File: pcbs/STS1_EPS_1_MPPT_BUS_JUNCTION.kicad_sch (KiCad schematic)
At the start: 26 parts, among them Q2 SI7135DP-T1-GE3, Q3 SI7135DP-T1-GE3, U11 INA180A4, U13 TPS259472ARPW, U19 TPS259472ARPW, U20 TPS259472ARPW, U21 TPS259472ARPW, U22 TPS259472ARPW, U23 TPS259472ARPW, U24 TPS259472ARPW, U4 TPS259472ARPW

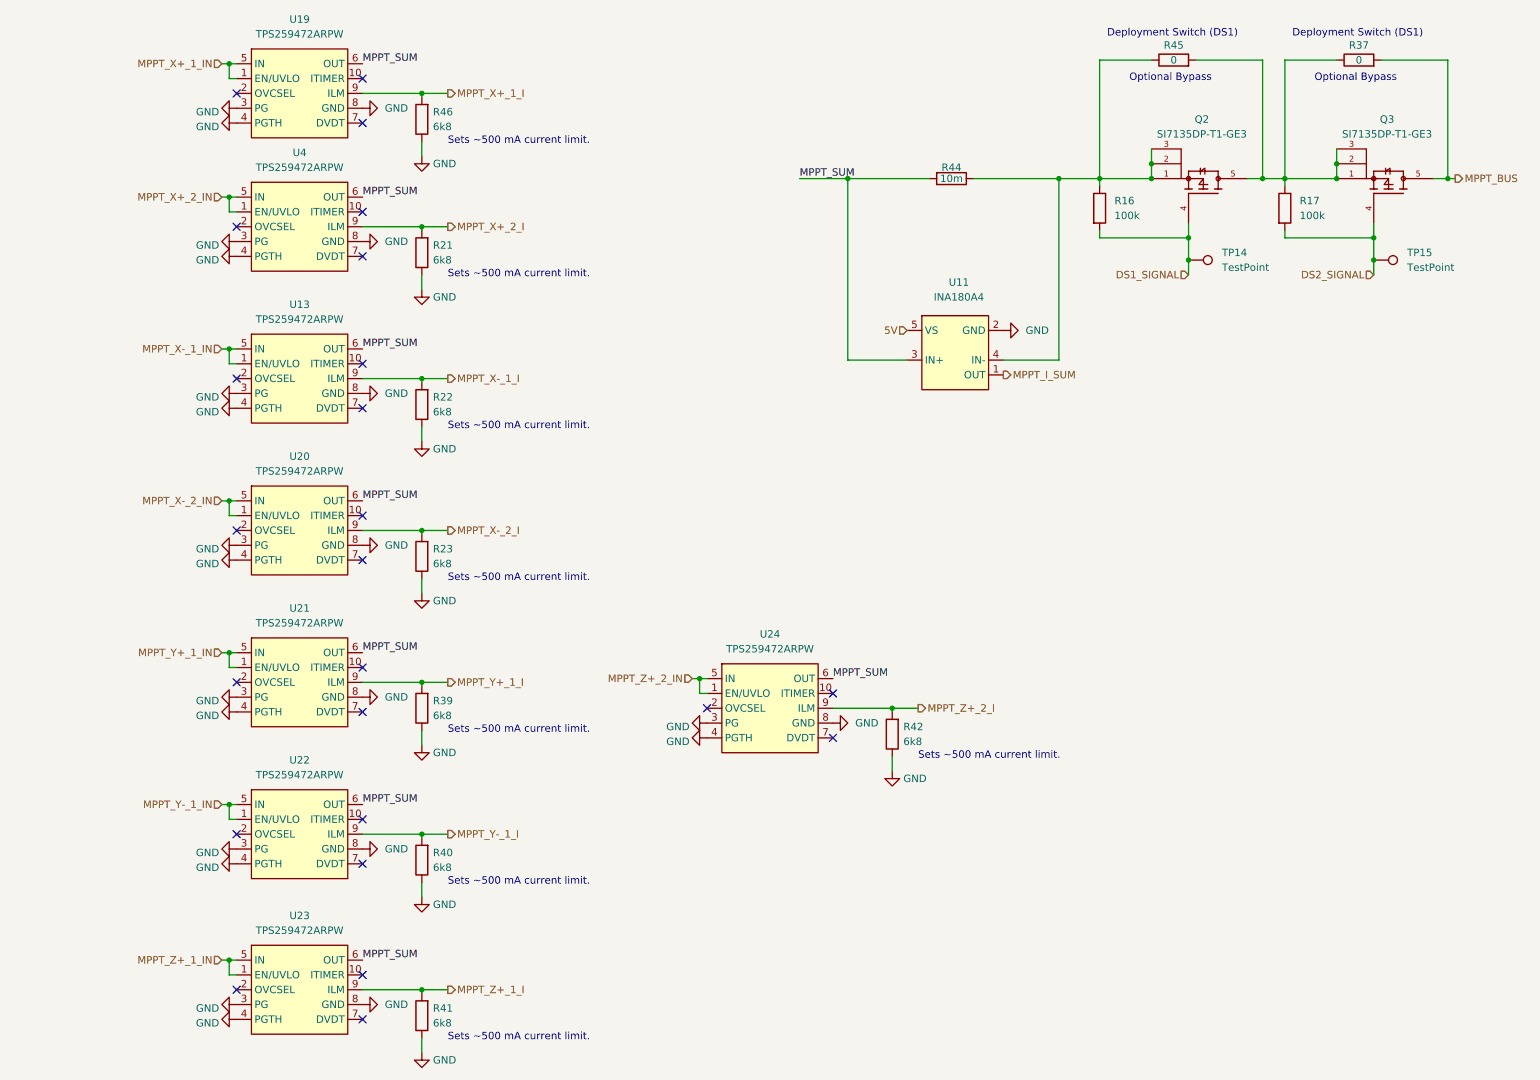
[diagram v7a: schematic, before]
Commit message: Worked on STS1_EPS_1.
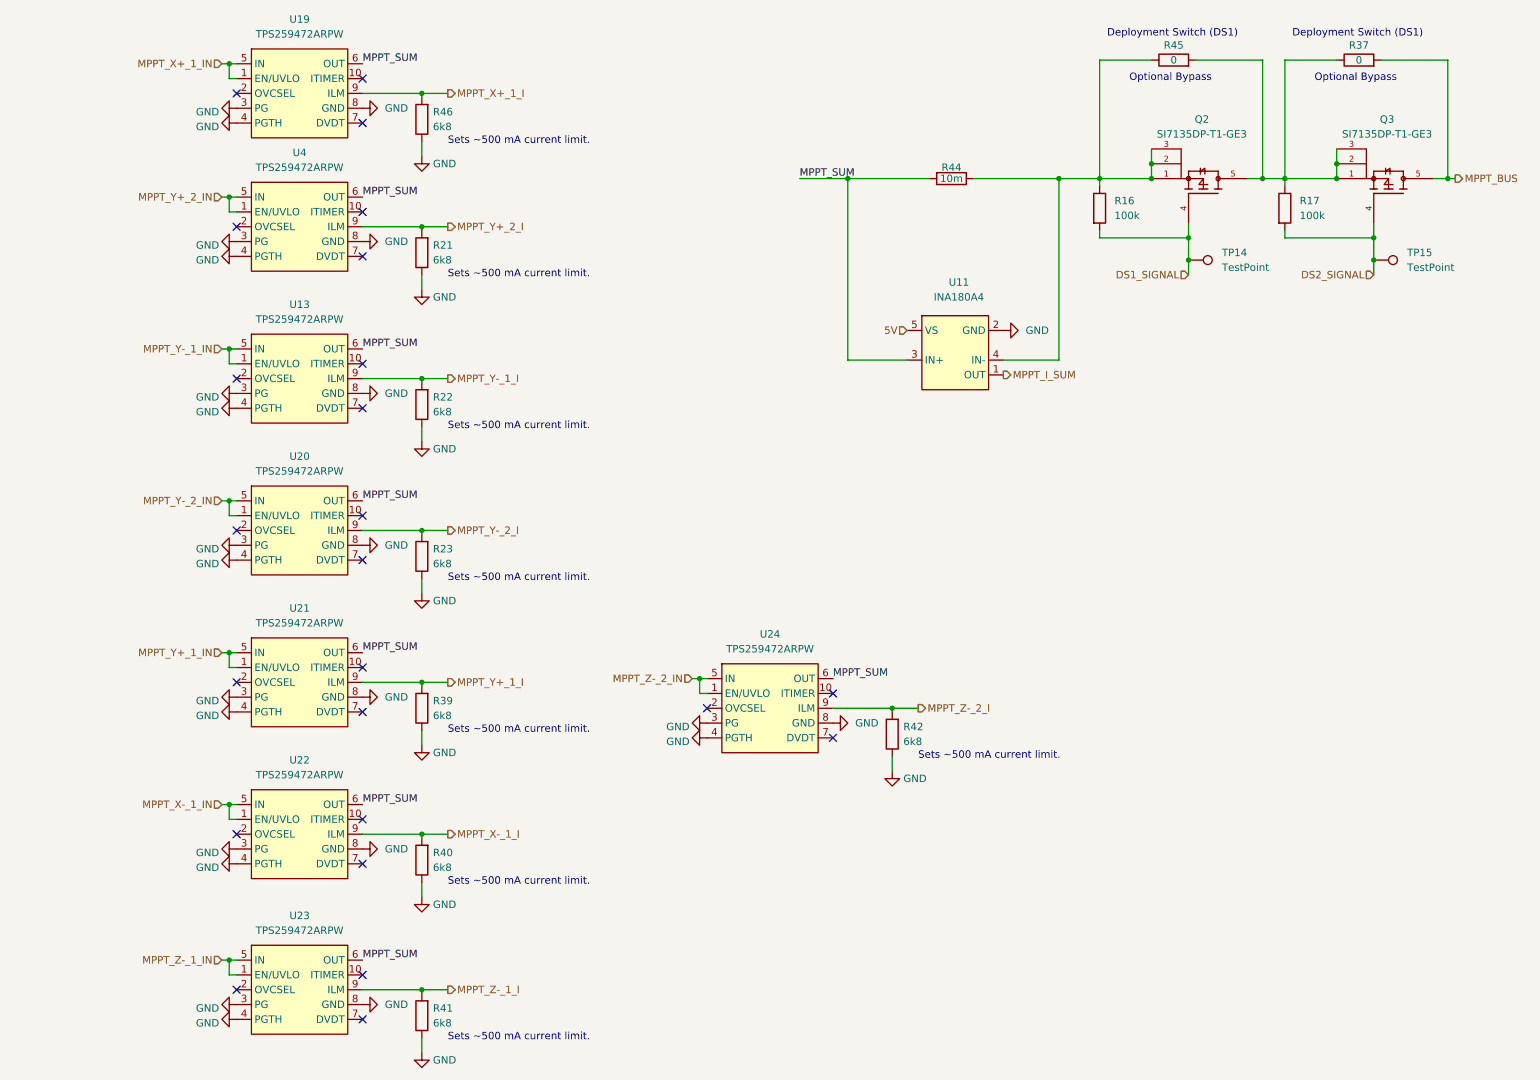
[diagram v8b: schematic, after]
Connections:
- net MPPT_X-_1_I: now also R40.2, U22.9 (ILM); no longer R22.2, U13.9 (ILM)
- net MPPT_X-_1_IN: now also U22.1 (EN/UVLO), U22.5 (IN); no longer U13.1 (EN/UVLO), U13.5 (IN)
- net MPPT_Y-_1_I: now also R22.2, U13.9 (ILM); no longer R40.2, U22.9 (ILM)
- net MPPT_Y-_1_IN: now also U13.1 (EN/UVLO), U13.5 (IN); no longer U22.1 (EN/UVLO), U22.5 (IN)
- net MPPT_X+_2_I renamed MPPT_Y+_2_I
- net MPPT_X+_2_IN renamed MPPT_Y+_2_IN
- net MPPT_X-_2_I renamed MPPT_Y-_2_I
- net MPPT_X-_2_IN renamed MPPT_Y-_2_IN
- net MPPT_Z+_1_I renamed MPPT_Z-_1_I
- net MPPT_Z+_1_IN renamed MPPT_Z-_1_IN
- net MPPT_Z+_2_I renamed MPPT_Z-_2_I
- net MPPT_Z+_2_IN renamed MPPT_Z-_2_IN
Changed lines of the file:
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@@
     (effects (font (size 1.27 1.27)) (justify left))
   )
-  (hierarchical_label "MPPT_Y-_1_I" (shape output) (at 86.36 155.575 0)
+  (hierarchical_label "MPPT_X-_1_I" (shape output) (at 86.36 155.575 0)
     (effects (font (size 1.27 1.27)) (justify left))
   )
-  (hierarchical_label "MPPT_Z+_1_I" (shape output) (at 86.36 182.245 0)
+  (hierarchical_label "MPPT_Z-_1_I" (shape output) (at 86.36 182.245 0)
     (effects (font (size 1.27 1.27)) (justify left))
   )
@@
     (effects (font (size 1.27 1.27)) (justify right))
   )
-  (hierarchical_label "MPPT_Z+_2_I" (shape output) (at 167.005 133.985 0)
+  (hierarchical_label "MPPT_Z-_2_I" (shape output) (at 167.005 133.985 0)
     (effects (font (size 1.27 1.27)) (justify left))
   )
@@
     (effects (font (size 1.27 1.27)) (justify left))
   )
-  (hierarchical_label "MPPT_Z+_2_IN" (shape input) (at 128.27 128.905 180)
+  (hierarchical_label "MPPT_Z-_2_IN" (shape input) (at 128.27 128.905 180)
     (effects (font (size 1.27 1.27)) (justify right))
   )
@@
     (effects (font (size 1.27 1.27)) (justify left))
   )
-  (hierarchical_label "MPPT_X+_2_I" (shape output) (at 86.36 51.435 0)
+  (hierarchical_label "MPPT_Y+_2_I" (shape output) (at 86.36 51.435 0)
     (effects (font (size 1.27 1.27)) (justify left))
   )
-  (hierarchical_label "MPPT_X-_2_IN" (shape input) (at 47.625 98.425 180)
+  (hierarchical_label "MPPT_Y-_2_IN" (shape input) (at 47.625 98.425 180)
     (effects (font (size 1.27 1.27)) (justify right))
   )
@@
     (effects (font (size 1.27 1.27)) (justify right))
   )
-  (hierarchical_label "MPPT_Y-_1_IN" (shape input) (at 47.625 150.495 180)
+  (hierarchical_label "MPPT_X-_1_IN" (shape input) (at 47.625 150.495 180)
     (effects (font (size 1.27 1.27)) (justify right))
   )
@@
     (effects (font (size 1.27 1.27)) (justify left))
   )
-  (hierarchical_label "MPPT_Z+_1_IN" (shape input) (at 47.625 177.165 180)
+  (hierarchical_label "MPPT_Z-_1_IN" (shape input) (at 47.625 177.165 180)
     (effects (font (size 1.27 1.27)) (justify right))
   )
-  (hierarchical_label "MPPT_X-_2_I" (shape output) (at 86.36 103.505 0)
+  (hierarchical_label "MPPT_Y-_2_I" (shape output) (at 86.36 103.505 0)
     (effects (font (size 1.27 1.27)) (justify left))
   )
-  (hierarchical_label "MPPT_X+_2_IN" (shape input) (at 47.625 46.355 180)
+  (hierarchical_label "MPPT_Y+_2_IN" (shape input) (at 47.625 46.355 180)
     (effects (font (size 1.27 1.27)) (justify right))
   )
@@
     (effects (font (size 1.27 1.27)) (justify right))
   )
-  (hierarchical_label "MPPT_X-_1_IN" (shape input) (at 47.625 72.39 180)
+  (hierarchical_label "MPPT_Y-_1_IN" (shape input) (at 47.625 72.39 180)
     (effects (font (size 1.27 1.27)) (justify right))
   )
-  (hierarchical_label "MPPT_X-_1_I" (shape output) (at 86.36 77.47 0)
+  (hierarchical_label "MPPT_Y-_1_I" (shape output) (at 86.36 77.47 0)
     (effects (font (size 1.27 1.27)) (justify left))
   )
